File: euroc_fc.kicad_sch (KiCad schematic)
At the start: 144 parts, among them J1 Micro-Fit, J10 USB_C_Receptacle_USB2.0, J2 Micro-Fit, J3 Micro-Fit, J4 SMA, J5 JST-GH, J6 JST-GH, J7 JST-GH, J8 JST-GH, J9 Micro_SD_Card_Det, Q1 DMN2056U, Q2 AOSP21321, Q3 DMN2056U, Q4 AOSP21321, Q5 DMN2056U, Q6 DMN2056U, Q7 DMN2056U, SW1 EVQ-PUC02K, SW2 EVQ-PUC02K, U1 STM32F401RCT6, U10 Ai-Thinker-Ra-01, U11 W25Q256JVF, U2 L7805, U3 L7805, U4 AZ1117I-3.3, U5 LSM6DSR, U6 ADXL375, U7 MS5611-01BA, U8 BMM150, U9 SAM-M8Q, Y1 25M

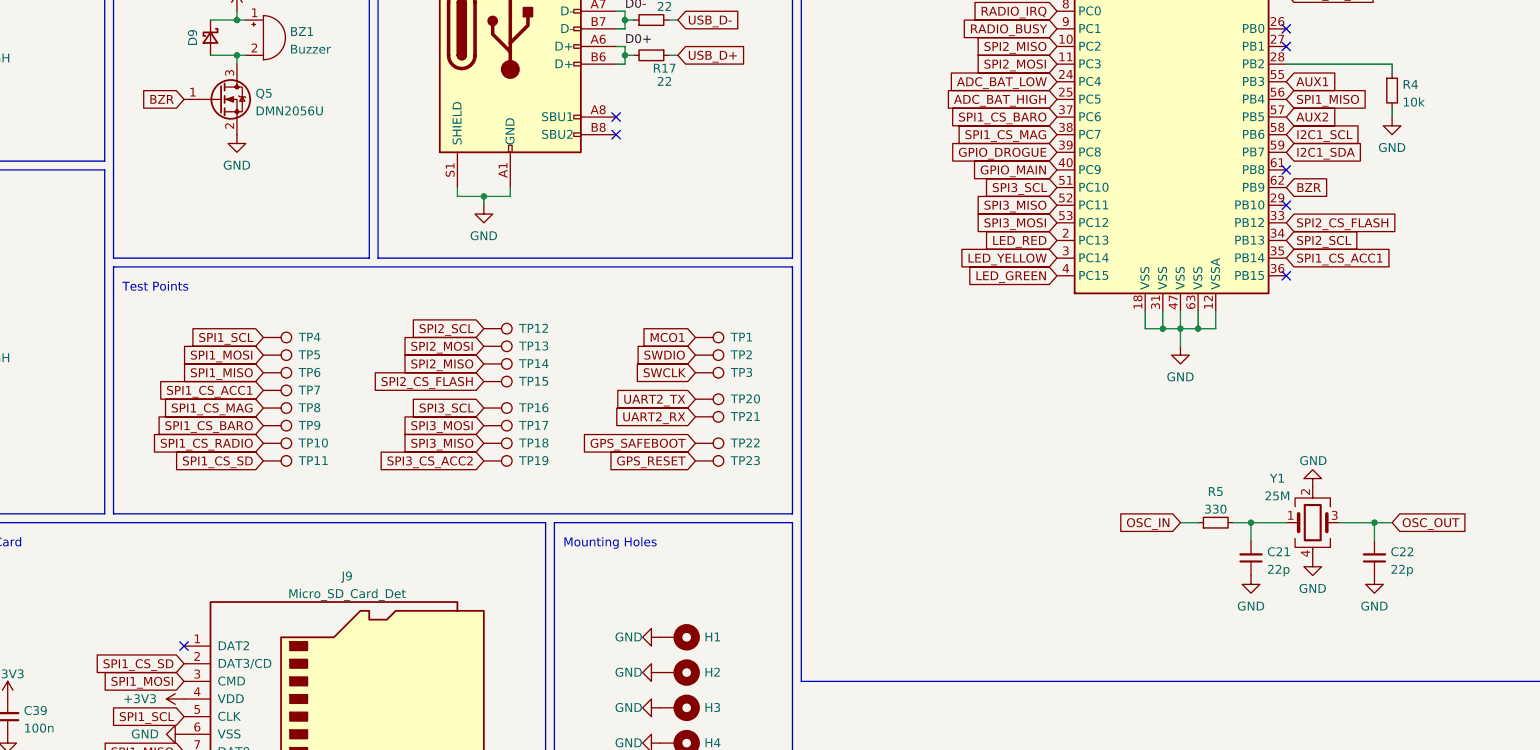
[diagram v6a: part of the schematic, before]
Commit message: Relayout the board, optimize return current paths
- Board stackup changed to Signal, Ground, Signal+Power, Signal+Ground
- L2 is now uninterrupted ground plane
- Addition of a proper SWD header (SWD test points removed)
- Moved all auxilliary connectors to the left
- Optimized paths for high-speed signals (SPI, SWD, USB)
- All SPI1 devices grouped on the left, SPI2 & 3 on the right, meaning
  shorter SPI1 bus
- No crossing of high speed signals on L1&2 or L3&4
- Addition of an indicator for coordinate system
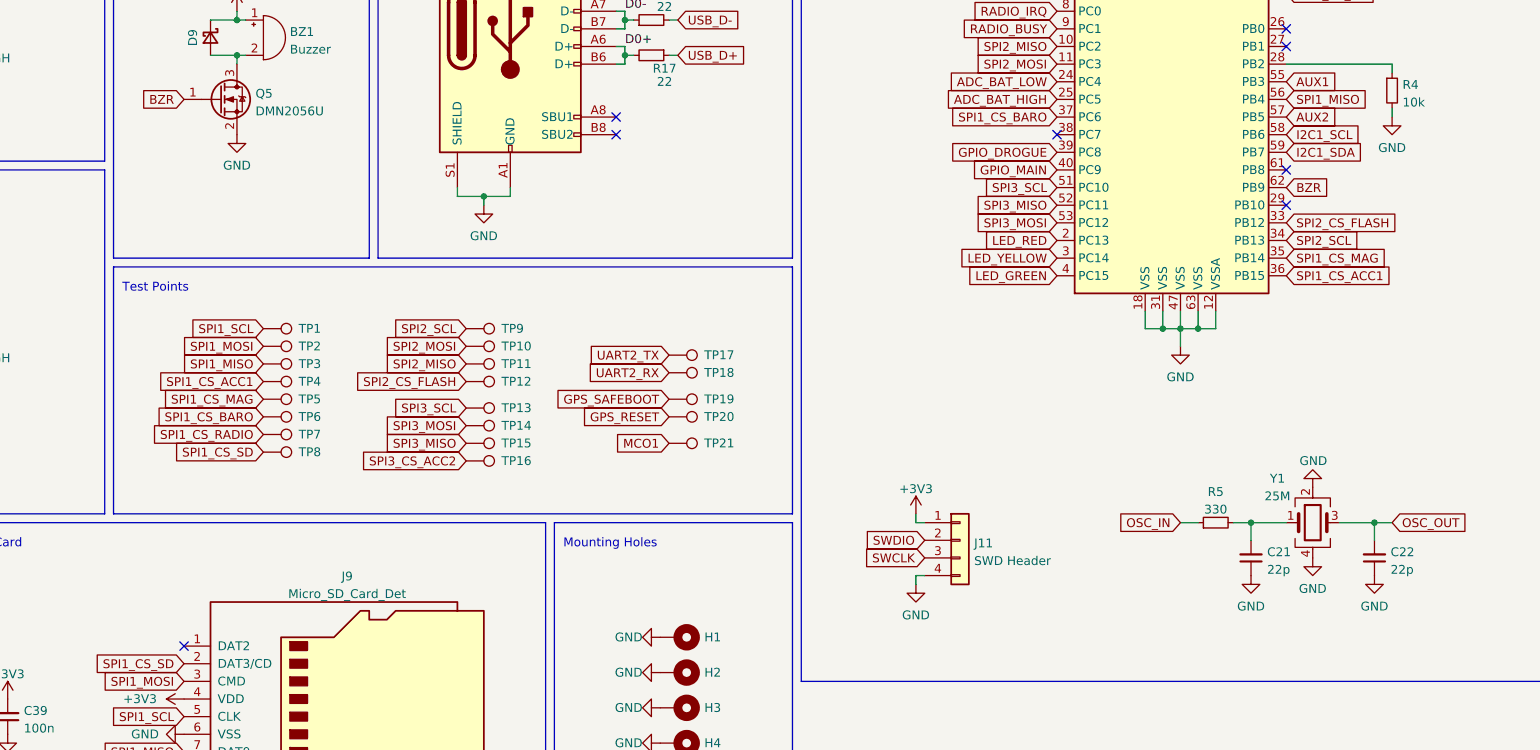
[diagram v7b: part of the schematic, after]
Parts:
- removed TP2, TP3: TestPoint, TestPoint:TestPoint_Pad_D1.0mm, symbol Connector:TestPoint
- added J11: SWD Header, Connector_PinHeader_2.54mm:PinHeader_1x04_P2.54mm_Vertical, symbol Connector_Generic:Conn_01x04
- renumbered TP4 to TP1, TP13 to TP10, TP14 to TP11, TP15 to TP12, TP16 to TP13, TP17 to TP14, TP18 to TP15, TP19 to TP16, TP20 to TP17, TP21 to TP18, TP22 to TP19, TP5 to TP2, TP23 to TP20, TP1 to TP21, TP6 to TP3, TP7 to TP4, TP8 to TP5, TP9 to TP6, TP10 to TP7, TP11 to TP8, TP12 to TP9
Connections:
- net +3V3: now also J11.1 (Pin_1)
- net GND: now also J11.4 (Pin_4)
- net SPI1_CS_ACC1: now also U1.36 (PB15); no longer U1.35 (PB14)
- net SPI1_CS_MAG: now also U1.35 (PB14); no longer U1.38 (PC7)
- net SWCLK: now also J11.3 (Pin_3)
- net SWDIO: now also J11.2 (Pin_2)
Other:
- moved on the sheet: TP1, TP10, TP11, TP12, TP13, TP14, TP15, TP16, TP17, TP18, TP19, TP2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

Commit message: Adjust cap value notation
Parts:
- C12: value 4.7u -> 4u7
- C20, C23: value 2.2u -> 2u2
- R18, R19: value 5.1k -> 5k1
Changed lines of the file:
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@@
     (in_bom yes) (on_board yes)
     (property "Reference" "R19" (id 0) (at 274.32 148.59 90))
-    (property "Value" "5.1k" (id 1) (at 281.94 148.59 90))
+    (property "Value" "5k1" (id 1) (at 281.94 148.59 90))
     (property "Footprint" "Resistor_SMD:R_0603_1608Metric" (id 2) (at 278.13 149.86 0)
       (effects (font (size 1.27 1.27)) hide)
@@
       (effects (font (size 1.27 1.27)) (justify right))
     )
-    (property "Value" "2.2u" (id 1) (at 332.74 121.92 90)
+    (property "Value" "2u2" (id 1) (at 332.74 121.92 90)
       (effects (font (size 1.27 1.27)) (justify left))
     )
@@
       (effects (font (size 1.27 1.27)) (justify right))
     )
-    (property "Value" "4.7u" (id 1) (at 314.7441 35.9858 0)
+    (property "Value" "4u7" (id 1) (at 314.7441 35.9858 0)
       (effects (font (size 1.27 1.27)) (justify right))
     )
@@
     (in_bom yes) (on_board yes)
     (property "Reference" "R18" (id 0) (at 274.32 146.05 90))
-    (property "Value" "5.1k" (id 1) (at 281.94 146.05 90))
+    (property "Value" "5k1" (id 1) (at 281.94 146.05 90))
     (property "Footprint" "Resistor_SMD:R_0603_1608Metric" (id 2) (at 278.13 147.32 0)
       (effects (font (size 1.27 1.27)) hide)
@@
       (effects (font (size 1.27 1.27)) (justify right))
     )
-    (property "Value" "2.2u" (id 1) (at 313.4741 79.1658 0)
+    (property "Value" "2u2" (id 1) (at 313.4741 79.1658 0)
       (effects (font (size 1.27 1.27)) (justify right))
     )
@@
     )
     (path "/d34756d8-5348-4c3c-a531-f319e4bdb91a"
-      (reference "C12") (unit 1) (value "4.7u") (footprint "Capacitor_SMD:C_1206_3216Metric")
+      (reference "C12") (unit 1) (value "4u7") (footprint "Capacitor_SMD:C_1206_3216Metric")
     )
     (path "/3cd7f773-0a10-4e28-b885-6073d1696a2c"
@@
     )
     (path "/d273d861-fe9a-47e0-ba73-de91dad4e413"
-      (reference "C20") (unit 1) (value "2.2u") (footprint "Capacitor_SMD:C_0805_2012Metric")
+      (reference "C20") (unit 1) (value "2u2") (footprint "Capacitor_SMD:C_0805_2012Metric")
     )
     (path "/b95d9e92-5ce1-4d92-b895-c83c1d047da7"
@@
     )
     (path "/f079ea11-5e21-4c6f-a1d7-701c3279e992"
-      (reference "C23") (unit 1) (value "2.2u") (footprint "Capacitor_SMD:C_0805_2012Metric")
+      (reference "C23") (unit 1) (value "2u2") (footprint "Capacitor_SMD:C_0805_2012Metric")
     )
     (path "/554e4252-d1f0-42ed-891f-58356c455d9d"
@@
     )
     (path "/dce81105-d9b3-4fea-ad8a-15b7d247a335"
-      (reference "R18") (unit 1) (value "5.1k") (footprint "Resistor_SMD:R_0603_1608Metric")
+      (reference "R18") (unit 1) (value "5k1") (footprint "Resistor_SMD:R_0603_1608Metric")
     )
     (path "/67b08e24-d33d-47a4-8a0a-66725323eede"
-      (reference "R19") (unit 1) (value "5.1k") (footprint "Resistor_SMD:R_0603_1608Metric")
+      (reference "R19") (unit 1) (value "5k1") (footprint "Resistor_SMD:R_0603_1608Metric")
     )
     (path "/3f2ec56e-2779-4c45-a385-86ee02356087"
